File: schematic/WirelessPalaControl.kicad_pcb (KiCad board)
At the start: 2 copper layers, 25.4 x 33.7 mm, 20 parts, among them J1 6P6C, J2 MCU UART, Q1 BC847B, Q2 BC847B, U1 SI8621, U2 WeMos_mini

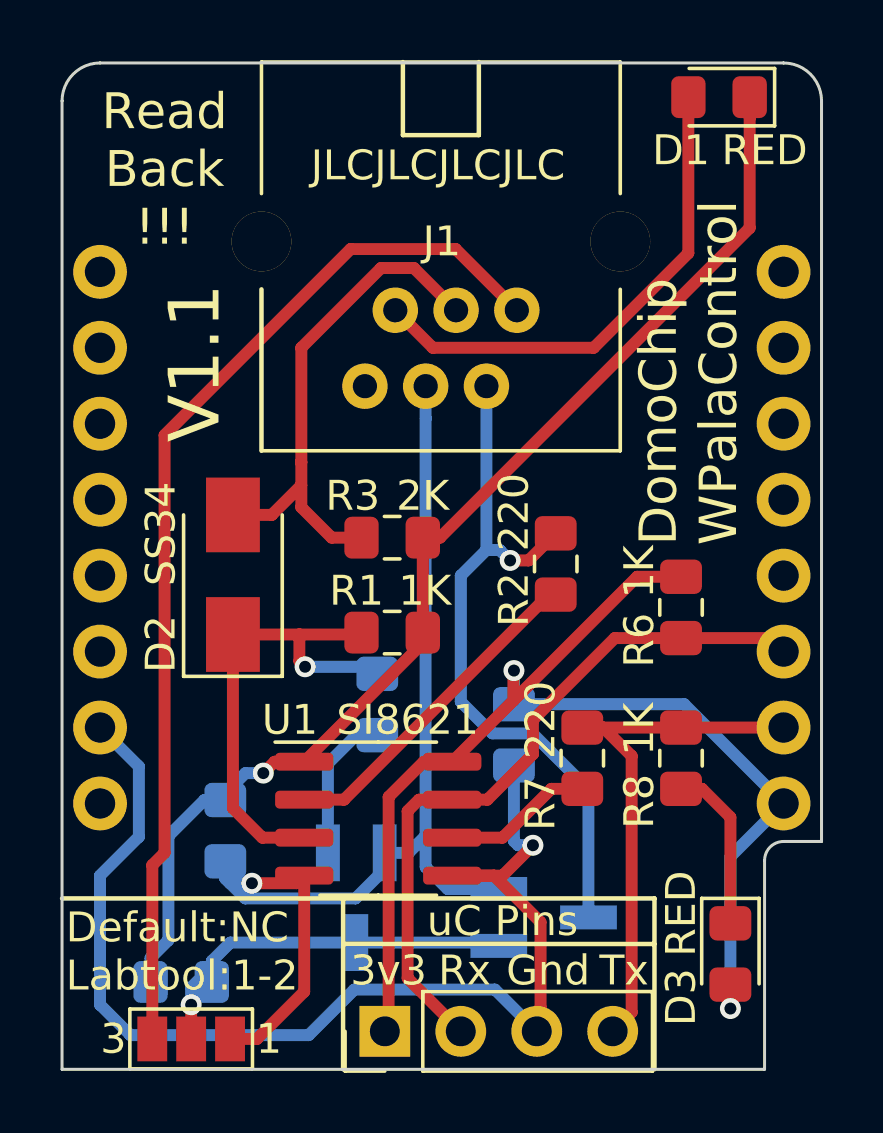
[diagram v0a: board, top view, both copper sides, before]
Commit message: Update schematic to KiCAD8
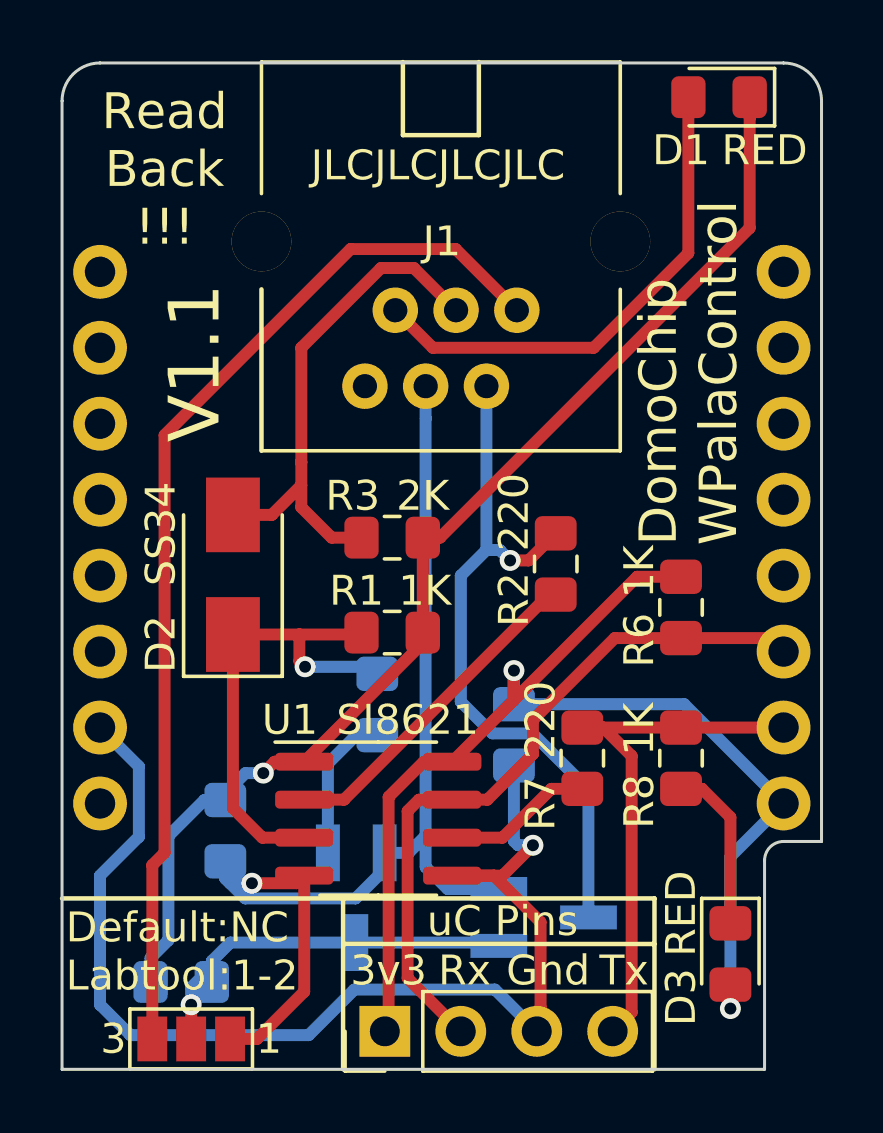
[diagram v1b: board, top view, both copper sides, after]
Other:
- net class Default removed
